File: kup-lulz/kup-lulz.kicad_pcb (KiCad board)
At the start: 4 copper layers, 154.5 x 137 mm, 340 parts, among them J1 CONN_PCIE_PWR_8PIN, J10 SFP_CAGE, J11 CONN_SFP_HOST, J12 SFP_CAGE, J13 PMOD_HOST, J14 PMOD_HOST, J15 CONN_QSFP_HOST, J16 CONN_QSFP_HOST, J17 SMPM, J18 SMPM, J19 SMPM, J2 CONN_IBC_MGMT, J20 SMPM, J21 SMPM, J22 SMPM, J23 SMPM, J24 SMPM, J25 SMPM, J26 SMPM, J27 SMPM, J28 SMPM, J29 SMPM, J3 CONN_01X03, J30 SMPM, J31 SMPM, J32 SMPM, J33 CONN_SFP_HOST, J34 SFP_CAGE, J35 QSFP_CAGE, J36 QSFP_CAGE, J37 XILINX_JTAG, J38 PMOD_HOST, J39 CONN_01X03, J4 CONN_01X05, J5 JUMPER_0402, J6 XILINX_JTAG, J7 CONN_SFP_HOST, J8 SFP_CAGE, J9 CONN_SFP_HOST, M1 HEATSINK, M2 SCREWHOLE, M3 SCREWHOLE, M4 SCREWHOLE, M5 SCREWHOLE, M6 LOGO, M7 LOGO, M8 LOGO, M9 LOGO, Q1 SSM6N58NU, SW1 SWITCH, SW2 SWITCH, U1 STM32L031C6U6, U10 MT25QU256ABA8E12-0AUT, U11 74LVC1T45, U12 74LVC1T45, U13 74LVC1T45, U14 STM32L431VxIx, U15 AT24MAC402, U16 SIT9121AI-2BF-XXS156.250000G, U17 SIT9121AI-2BF-XXS156.250000G, U18 SIT9121AI-2BF-XXS156.250000G, U2 MYMGK1R812ERSR, U3 MYMGK1R812ERSR, U4 MYMGK00506ERSR, U5 MYMGK00504ERSR, U7 MYMGK00504ERSR, U8 ADP1740ACPZ-1.8-R7, U9 XILINX_ULTRASCALEPLUS_B676

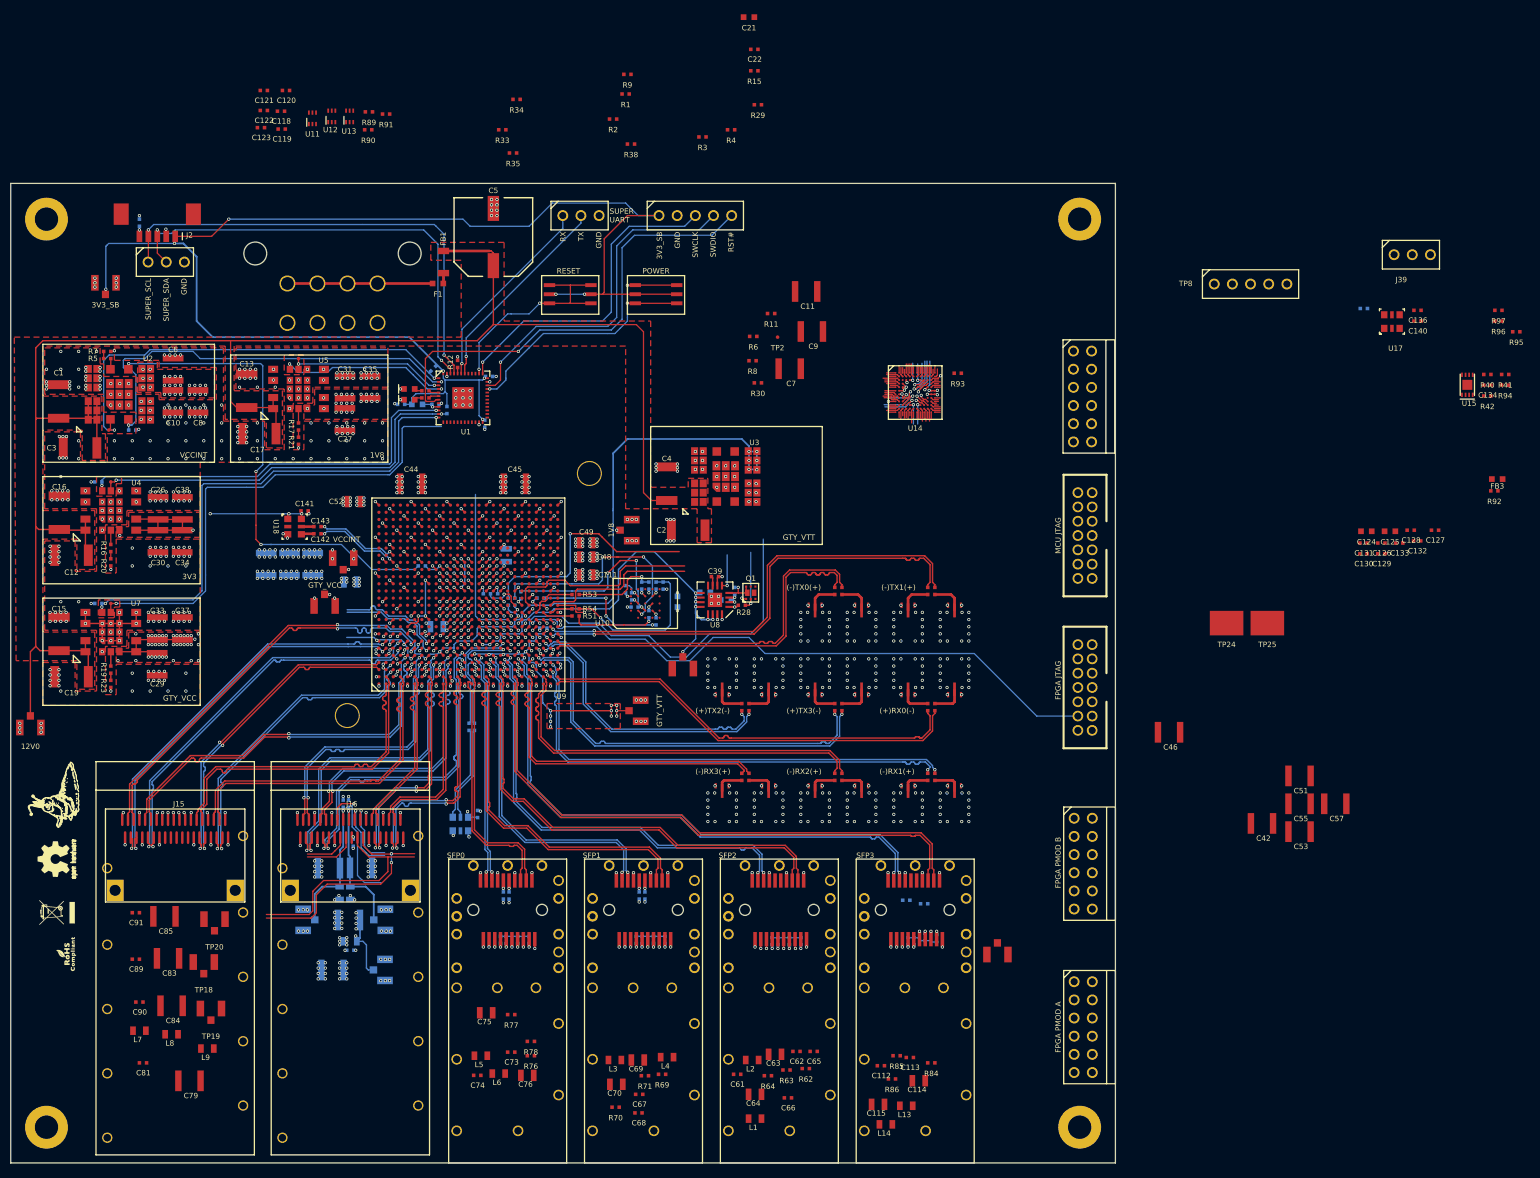
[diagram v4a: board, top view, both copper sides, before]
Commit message: Continued kup-lulz routing. Deleted one of the PMODs as there's no way it will fit.
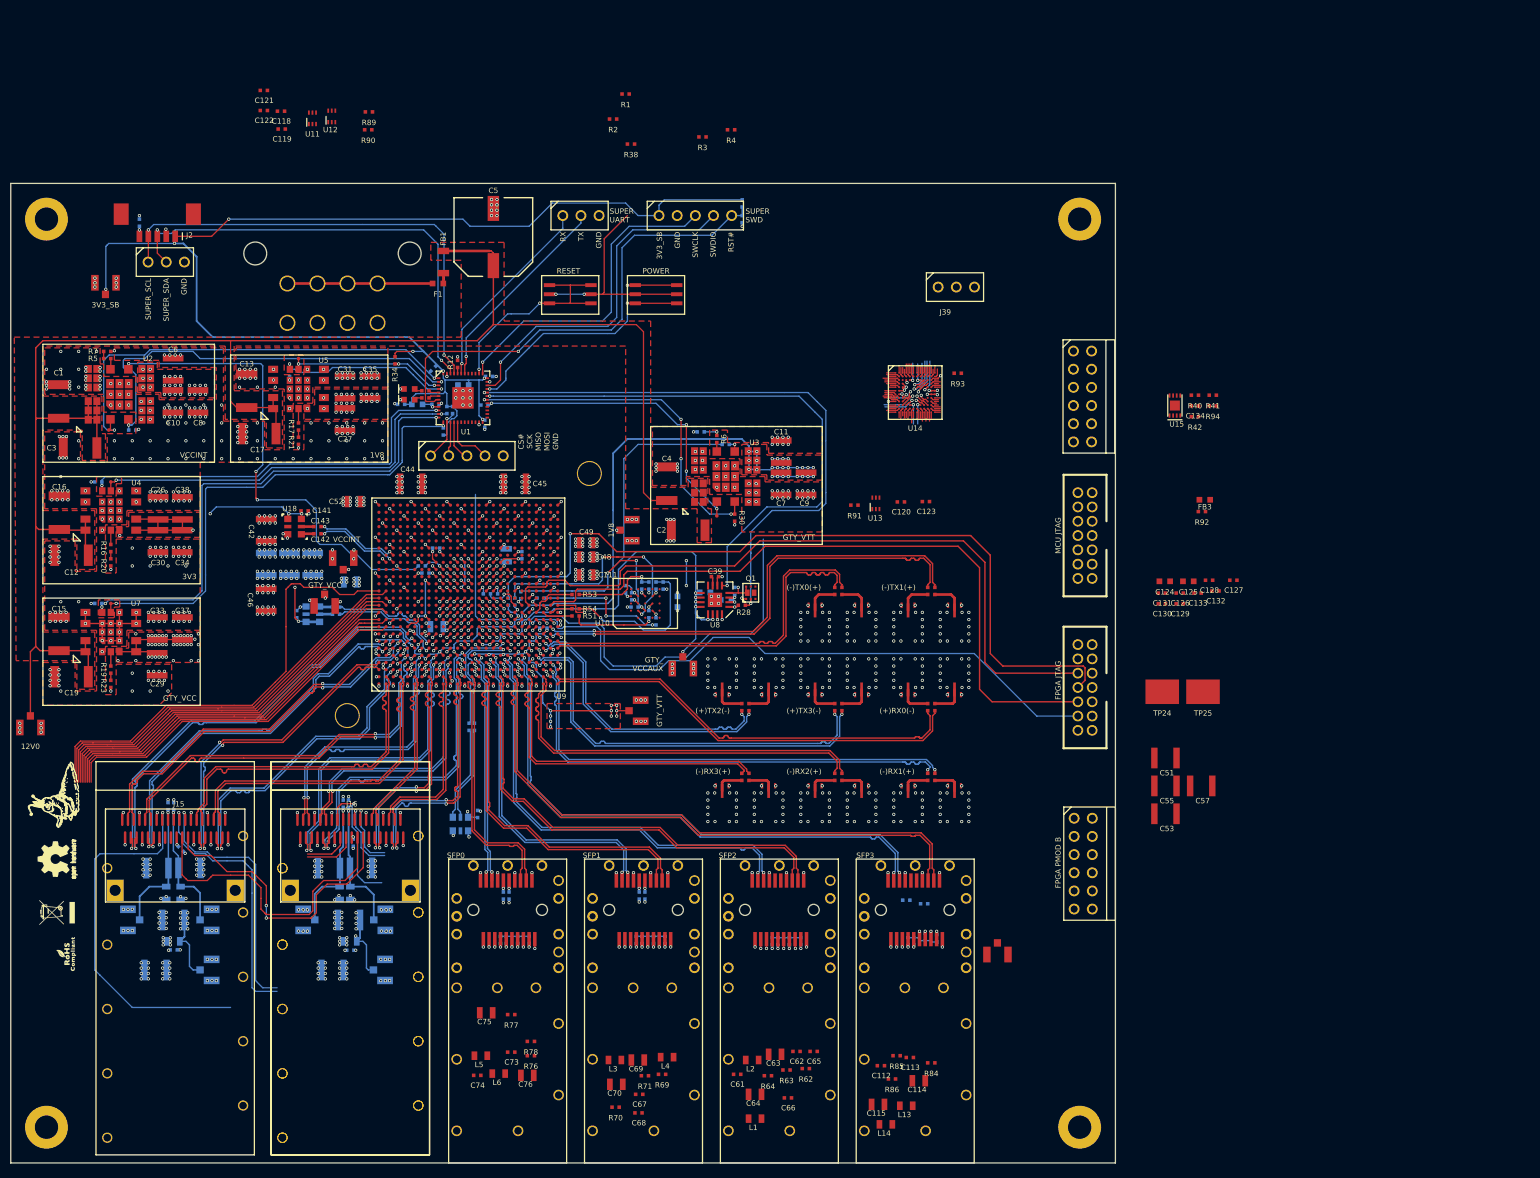
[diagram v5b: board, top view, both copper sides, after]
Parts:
- removed J13: PMOD_HOST, azonenberg_pcb:CONN_HEADER_2.54MM_2x6_RA_PMOD_HOST
- added J36: QSFP_CAGE, azonenberg_pcb:CONN_ZQSFP+_CAGE_TE_4-2170705-5, F.Cu at (68.0, 122.9)
- C136, C140, C21, C22, C79, C81, C83, C84, C85, C89, C90, C91, L7, L8, L9, R11, R15, R29, R33, R35, R8, R9, R95, R96, R97, TP18, TP19, TP20, U17: moved to B.Cu
- moved C136 162.4 mm to (60.5, 84.2), turned to 90 degrees
- moved C140 156.7 mm to (66.0, 84.2)
- moved U17 156.4 mm to (62.8, 84.2), turned to 90 degrees
- moved R95 156.3 mm to (78.5, 78.5)
- moved R96 151.9 mm to (80.0, 75.0), turned to 180 degrees
- moved C139 149.7 mm to (66.0, 83.2), turned to 0 degrees
- moved C42 145.2 mm to (56.2, 72.5), turned to -90 degrees
- moved R97 140.8 mm to (92.0, 76.0), turned to -90 degrees
- moved C46 127.6 mm to (56.2, 82.2), turned to -90 degrees
- moved TP8 112.2 mm to (84.3, 62.1)
- moved C123 106.7 mm to (148.5, 68.5)
- moved C120 103.5 mm to (145.0, 68.5)
- moved U13 91.4 mm to (141.5, 68.8)
- moved R91 85.3 mm to (138.5, 69.0)
- moved C21 65.1 mm to (83.8, 52.2), turned to 180 degrees
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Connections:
- J15 pad 2: /QSFP28 interface/QSFP28A_TX4_P -> /QSFP28 interface/QSFP28A_TX1_P
- J15 pad 3: /QSFP28 interface/QSFP28A_TX4_N -> /QSFP28 interface/QSFP28A_TX1_N
- J15 pad 36: /QSFP28 interface/QSFP28A_TX1_P -> /QSFP28 interface/QSFP28A_TX3_N
- J15 pad 37: /QSFP28 interface/QSFP28A_TX1_N -> /QSFP28 interface/QSFP28A_TX3_P
- J15 pad 5: /QSFP28 interface/QSFP28A_TX3_P -> /QSFP28 interface/QSFP28A_TX4_P
- J15 pad 6: /QSFP28 interface/QSFP28A_TX3_N -> /QSFP28 interface/QSFP28A_TX4_N
- TP8 pad 3: /Power Supply/SUPER_SPI_MOSI -> /Power Supply/SUPER_SPI_MISO
- TP8 pad 4: /Power Supply/SUPER_SPI_MISO -> /Power Supply/SUPER_SPI_MOSI
- U1 pad 13: unconnected-(U1-Pad13) -> /Power Supply/GTY_VCC_PGOOD
- U1 pad 26: /Power Supply/GTY_VCC_PGOOD -> unconnected-(U1-Pad26)
- U1 pad 27: /Power Supply/GTY_VCCAUX_PGOOD -> unconnected-(U1-Pad27)
- U1 pad 28: /Power Supply/GTY_VCCAUX_EN_N -> unconnected-(U1-Pad28)
- U1 pad 31: unconnected-(U1-Pad31) -> /Power Supply/GTY_VCCAUX_PGOOD
- U1 pad 32: unconnected-(U1-Pad32) -> /Power Supply/GTY_VCCAUX_EN_N
- U14 pad B3: /Management/MCU_PMOD_DQ1 -> /Power Supply/SUPER_SPI_CS_N
- U14 pad B4: unconnected-(U14-PadB4) -> /Management/MCU_PMOD_DQ1
- U14 pad B5: unconnected-(U14-PadB5) -> /Management/MCU_PMOD_DQ5
- U14 pad D12: /Management/QSFP1_LPMODE -> /SFP28 interfaces/SFP1_I2C_SDA
- U14 pad E10: /Management/QSFP1_I2C_SEL_N -> unconnected-(U14-PadE10)
- U14 pad E11: /Management/QSFP1_PRESENT_N -> /Management/SFP0_MOD_ABS
- U14 pad E12: /Management/QSFP1_RST_N -> /Management/SFP0_RX_LOS
- U14 pad H1: /Management/QSFP0_INT_N -> unconnected-(U14-PadH1)
- U14 pad J2: /Management/QSFP0_RST_N -> unconnected-(U14-PadJ2)
- U14 pad J3: /Management/QSFP0_PRESENT_N -> unconnected-(U14-PadJ3)
- U14 pad K10: /Management/MCU_PMOD_DQ7 -> /Power Supply/SUPER_SPI_MOSI
- U14 pad K11: /Management/MCU_PMOD_DQ6 -> /Power Supply/SUPER_SPI_MISO
- U14 pad K12: /Management/MCU_PMOD_DQ5 -> /Power Supply/SUPER_SPI_SCK
- U14 pad K2: /Management/QSFP0_I2C_SEL_N -> unconnected-(U14-PadK2)
- U14 pad K5: /Management/QSFP0_LPMODE -> unconnected-(U14-PadK5)
- U14 pad L5: /Management/QSFP1_INT_N -> unconnected-(U14-PadL5)
- U14 pad M5: unconnected-(U14-PadM5) -> /Management/MCU_PMOD_DQ6
- U14 pad M6: unconnected-(U14-PadM6) -> /Management/MCU_PMOD_DQ7
- U9 pad A10: /Power Supply/SUPER_SPI_MISO -> /Management/QSFP0_PRESENT_N
- U9 pad A12: /Management/SFP0_RX_LOS -> /Management/QSFP1_RST_N
- U9 pad A13: /Management/SFP0_MOD_ABS -> /Management/QSFP1_PRESENT_N
- U9 pad A14: /SFP28 interfaces/SFP0_I2C_SDA -> /Management/QSFP1_INT_N
- U9 pad A9: unconnected-(U9-PadA9) -> /Management/QSFP0_LPMODE
- U9 pad AA13: /Management/PMOD_DQ2 -> unconnected-(U9-PadAA13)
- U9 pad B10: /Power Supply/SUPER_SPI_MOSI -> /Management/QSFP0_I2C_SEL_N
- U9 pad B11: /Power Supply/SUPER_SPI_CS_N -> /Management/QSFP1_I2C_SEL_N
- U9 pad B12: /SFP28 interfaces/SFP1_I2C_SDA -> /Management/QSFP1_LPMODE
- U9 pad B14: /SFP28 interfaces/SFP0_I2C_SCL -> /Management/QSFP0_RST_N
- U9 pad B9: unconnected-(U9-PadB9) -> /Management/QSFP0_INT_N
- U9 pad C11: /Power Supply/SUPER_SPI_SCK -> /SFP28 interfaces/SFP0_I2C_SCL
- U9 pad J15: unconnected-(U9-PadJ15) -> /SFP28 interfaces/SFP0_I2C_SDA
- U9 pad W12: /Management/PMOD_DQ1 -> unconnected-(U9-PadW12)
- U9 pad W13: /Management/PMOD_DQ0 -> unconnected-(U9-PadW13)
- U9 pad W14: /Management/PMOD_DQ5 -> unconnected-(U9-PadW14)
- U9 pad W15: /Management/PMOD_DQ4 -> unconnected-(U9-PadW15)
- U9 pad W16: /Management/PMOD_DQ7 -> unconnected-(U9-PadW16)
- U9 pad Y13: /Management/PMOD_DQ3 -> unconnected-(U9-PadY13)
- U9 pad Y16: /Management/PMOD_DQ6 -> unconnected-(U9-PadY16)
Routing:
- net /GND: track 2732.0 -> 2867.5 mm, vias 1055 -> 1156
- net /Management/QSFP0_LPMODE: track 4.23 -> 104.1 mm, vias 2 -> 1
- net /Management/QSFP0_INT_N: track 2.88 -> 88.9 mm
- net /Management/QSFP0_PRESENT_N: track 6.83 -> 88.5 mm, vias 2 -> 1
- net /Power Supply/GTY_VCCAUX_EN_N: track 8.64 -> 86.0 mm, vias 1 -> 2
- net /Power Supply/GTY_VCCAUX_PGOOD: track 5.03 -> 81.8 mm, vias 1 -> 2
- net /FPGA support/FPGA_JTAG_TDO: track 33.1 -> 109.7 mm
- net /FPGA support/FPGA_JTAG_TCK: track 22.3 -> 97.7 mm
- net /FPGA support/FPGA_JTAG_TDI: track 28.0 -> 100.3 mm
- net /GTY_VTT: track 146.0 -> 217.4 mm, vias 31 -> 53
- net /Management/QSFP1_INT_N: track 12.1 -> 75.0 mm
- net /Management/QSFP1_LPMODE: track 19.0 -> 74.4 mm
- net /Management/QSFP0_RST_N: track 2.32 -> 57.1 mm
- net /Management/QSFP1_PRESENT_N: track 11.0 -> 65.0 mm
- net /Management/QSFP1_RST_N: track 8.06 -> 61.4 mm
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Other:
- board text added: "CS# SCK MISO MOSI GND"
- board text added: "GTY_ VCCAUX"
- board text added: "SUPER SWD"
- board text added: "VCC1"
- board text added: "VCCRX"
- board text added: "VCCTX"
- board text removed: "FPGA PMOD A"

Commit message: Initial work on power planes, finished hooking up QSFP GPIOs
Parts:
- R3, R38, R4: moved to B.Cu
- moved R38 40.7 mm to (86.1, 53.3), turned to 90 degrees
- moved R3 26.9 mm to (99.2, 37.5), turned to 180 degrees
- moved R4 25.3 mm to (106.8, 37.3), turned to -90 degrees
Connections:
- U14 pad L10: /Management/QSFP_I2C_SCL -> unconnected-(U14-PadL10)
- U14 pad L11: /Management/QSFP_I2C_SDA -> unconnected-(U14-PadL11)
- U9 pad A10: /Management/QSFP0_PRESENT_N -> /Management/QSFP_I2C_SCL
- U9 pad A12: /Management/QSFP1_RST_N -> /Management/QSFP0_INT_N
- U9 pad A13: /Management/QSFP1_PRESENT_N -> /Management/QSFP1_I2C_SEL_N
- U9 pad A14: /Management/QSFP1_INT_N -> /Management/QSFP1_LPMODE
- U9 pad A9: /Management/QSFP0_LPMODE -> /Management/QSFP0_I2C_SEL_N
- U9 pad B10: /Management/QSFP0_I2C_SEL_N -> /Management/QSFP0_RST_N
- U9 pad B11: /Management/QSFP1_I2C_SEL_N -> /Management/QSFP_I2C_SDA
- U9 pad B12: /Management/QSFP1_LPMODE -> /Management/QSFP0_PRESENT_N
- U9 pad B14: /Management/QSFP0_RST_N -> /Management/QSFP1_RST_N
- U9 pad B9: /Management/QSFP0_INT_N -> /Management/QSFP0_LPMODE
- U9 pad C12: /SFP28 interfaces/SFP1_I2C_SCL -> /Management/QSFP1_INT_N
- U9 pad D10: unconnected-(U9-PadD10) -> /Management/SFP2_RX_LOS
- U9 pad E12: /Management/SFP2_RX_LOS -> /Management/QSFP1_PRESENT_N
- U9 pad J14: unconnected-(U9-PadJ14) -> /SFP28 interfaces/SFP1_I2C_SCL
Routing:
- net /Management/QSFP1_PRESENT_N: track 65.0 -> 183.6 mm, vias 1 -> 4
- net /Management/QSFP1_LPMODE: track 74.4 -> 176.9 mm, vias 1 -> 2
- net /Management/QSFP1_INT_N: track 75.0 -> 176.2 mm, vias 1 -> 4
- net /Management/QSFP_I2C_SDA: track 42.6 -> 139.3 mm
- net /Management/QSFP1_RST_N: track 61.4 -> 145.6 mm, vias 0 -> 2
- net /Management/QSFP1_I2C_SEL_N: track 60.9 -> 142.4 mm, vias 0 -> 2
- net /Management/QSFP_I2C_SCL: track 45.2 -> 122.6 mm
- net /Management/QSFP0_PRESENT_N: track 88.5 -> 143.0 mm, vias 1 -> 2
- net /Management/QSFP0_INT_N: track 88.9 -> 139.3 mm, vias 1 -> 2
- net /Management/QSFP0_LPMODE: track 104.1 -> 77.2 mm, vias 1 -> 2
- net /Management/QSFP0_RST_N: track 57.1 -> 77.2 mm
- net /Management/QSFP0_I2C_SEL_N: track 53.1 -> 73.2 mm, vias 0 -> 1
- net /GND: track 2867.5 -> 2879.7 mm, vias 1156 -> 1158
- net /FPGA support/FPGA_RESET_N: track 54.5 -> 65.9 mm
- net /FPGA support/1V8: track 292.7 -> 297.9 mm
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- added copper zone on In2.Cu, net /3V3
- added copper zone on In2.Cu, net /Power Supply/GTY_VCC
